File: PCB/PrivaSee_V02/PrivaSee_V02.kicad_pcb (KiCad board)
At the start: 2 copper layers, 76.2 x 101.6 mm, 18 parts, among them SW1 (Generic toggle state switch), U1 ESP32-C6-DevKitM-1, U2 LM358, U5 LM358

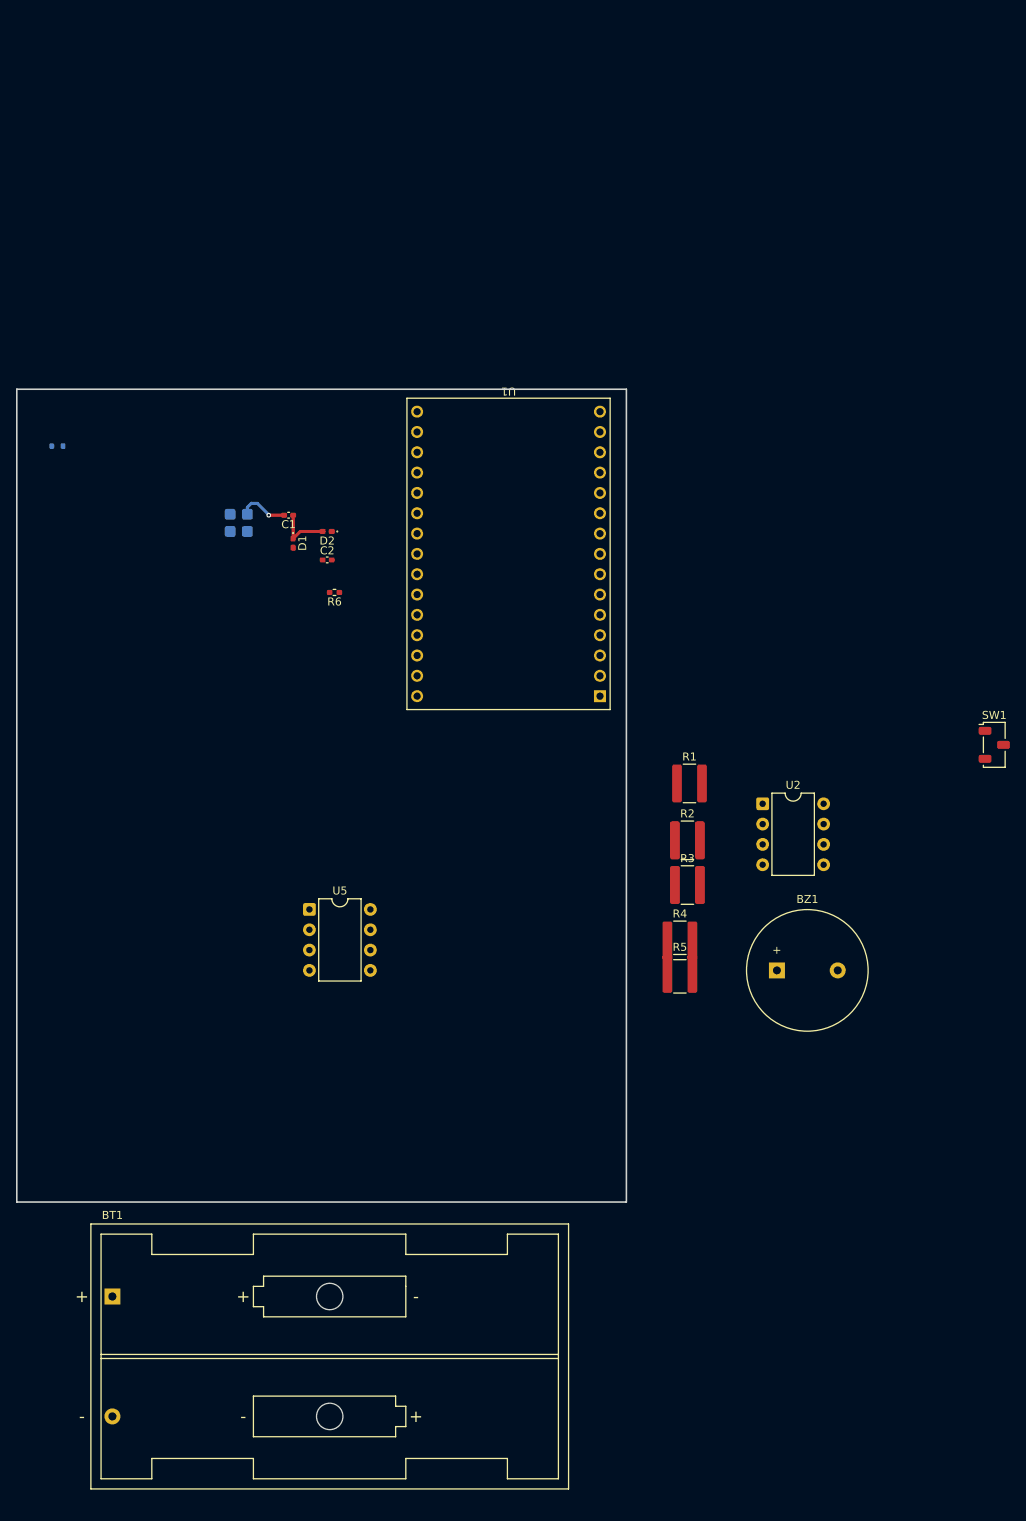
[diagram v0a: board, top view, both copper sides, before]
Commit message: PCB Layout Updates
Updated the footprint and the layout of the PCB
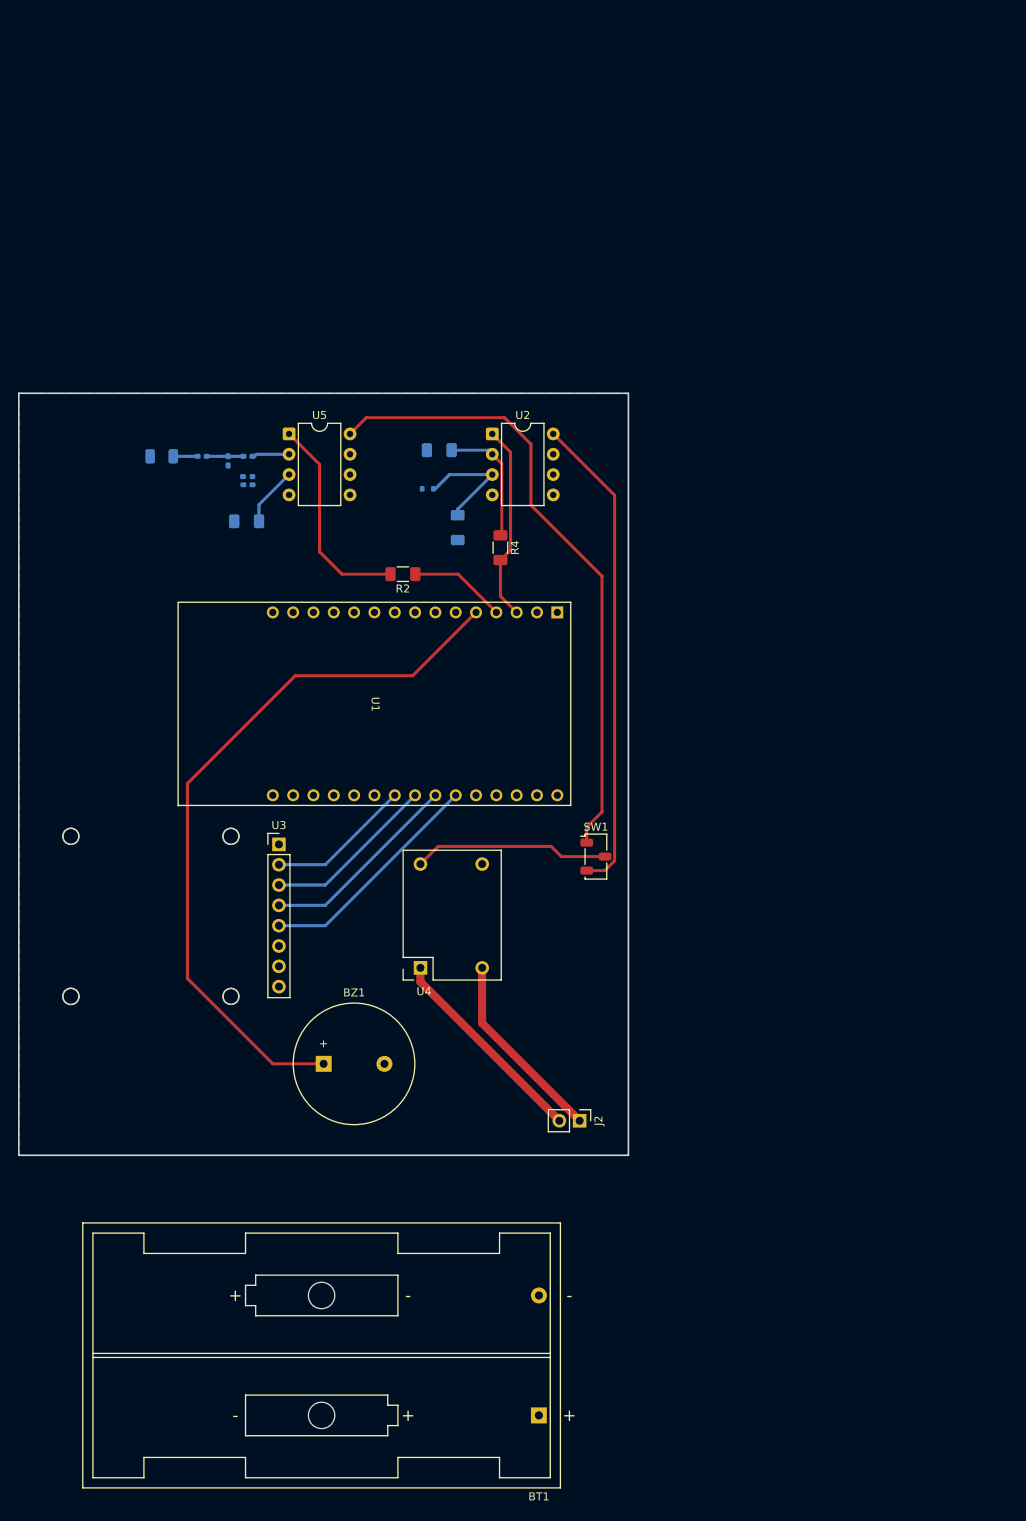
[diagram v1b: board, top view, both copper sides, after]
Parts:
- added J2: Batt_Solder_Point, Connector_PinHeader_2.54mm:PinHeader_1x02_P2.54mm_Vertical, F.Cu at (129.8, 112.5)
- added U3: 254, Connector_PinHeader_2.54mm:PinHeader_1x08_P2.54mm_Vertical, F.Cu at (92.2, 78.0)
- added U4: DFR0568, Connector_PinSocket_2.54mm:PinSocket_2x02_P2.54mm_Vertical, F.Cu at (109.1, 93.6)
- AE1: footprint RF_Antenna:Molex_47948-0001_2.4Ghz -> RF_Antenna:Johanson_2450AT18x100_2400-2500Mhz
- C1, C2, D1, D2, R6: moved to B.Cu
- R1, R3, R5: footprint Resistor_SMD:R_1218_3246Metric_Pad1.22x4.75mm_HandSolder -> Resistor_SMD:R_1206_3216Metric_Pad1.30x1.75mm_HandSolder; moved to B.Cu
- R2, R4: footprint Resistor_SMD:R_1218_3246Metric_Pad1.22x4.75mm_HandSolder -> Resistor_SMD:R_1206_3216Metric_Pad1.30x1.75mm_HandSolder
- moved R1 64.3 mm to (88.2, 37.6), turned to 180 degrees
- moved R3 62.6 mm to (112.2, 28.7)
- moved R5 62.3 mm to (114.6, 38.4), turned to 90 degrees
- moved U5 59.5 mm to (93.5, 26.7)
- moved BZ1 57.9 mm to (97.8, 105.4)
- moved U2 57.3 mm to (118.9, 26.7)
- moved BT1 55.3 mm to (124.7, 149.4), turned to 180 degrees
- moved R4 54.0 mm to (119.9, 40.9), turned to -90 degrees
- moved SW1 51.7 mm to (131.8, 79.5)
- moved R2 48.7 mm to (107.7, 44.2), turned to 180 degrees
- moved D3 46.6 mm to (110.8, 33.5)
- moved R6 18.1 mm to (88.3, 32.0)
- moved D2 13.7 mm to (88.3, 29.5)
- moved C2 13.7 mm to (88.3, 33.0)
- moved D1 13.1 mm to (85.9, 30.0)
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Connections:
- BZ1 pad 2: /GND -> GND
- C2 pad 1: /GND -> GND
- D1 pad 2: /GND -> GND
- D3 pad 2: /GND -> GND
- R1 pad 2: /GND -> GND
- R3 pad 1: /GND -> GND
- R5 pad 1: /GND -> GND
- R6 pad 2: /GND -> GND
- U1 pad 15: unconnected-(U1-GND-Pad15) -> GND
- U1 pad 16: unconnected-(U1-GND-Pad16) -> GND
- U1 pad 30: /GND -> GND
- U2 pad 4: /GND -> GND
- U5 pad 4: /GND -> GND
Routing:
- net Net-(BZ1-+): track 0.00 -> 90.7 mm
- net Net-(SW1-C): track 0.00 -> 79.1 mm
- net Net-(SW1-A): track 0.00 -> 60.5 mm
- net Net-(U1-GPIO21): track 0.00 -> 28.8 mm
- net Net-(R2-Pad2): track 0.00 -> 26.3 mm
- net Net-(BT1-+): track 0.00 -> 26.3 mm
- net Net-(U1-GPIO20): track 0.00 -> 25.3 mm
- net Net-(U1-GPIO2): track 0.00 -> 24.6 mm
- net Net-(SW1-B): track 0.00 -> 24.5 mm
- net Net-(BT1--): track 0.00 -> 24.2 mm
- net Net-(U1-GPIO19): track 0.00 -> 21.7 mm
- net Net-(U1-GPIO18): track 0.00 -> 18.1 mm
- net Net-(U2A--): track 0.00 -> 16.0 mm
- net Net-(D3-K): track 0.00 -> 15.0 mm
- net Net-(U1-GPIO3): track 0.00 -> 12.1 mm
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- added copper zone on B.Cu, net GND
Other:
- board size 76.2 x 101.6 mm -> 76.2 x 95.2 mm

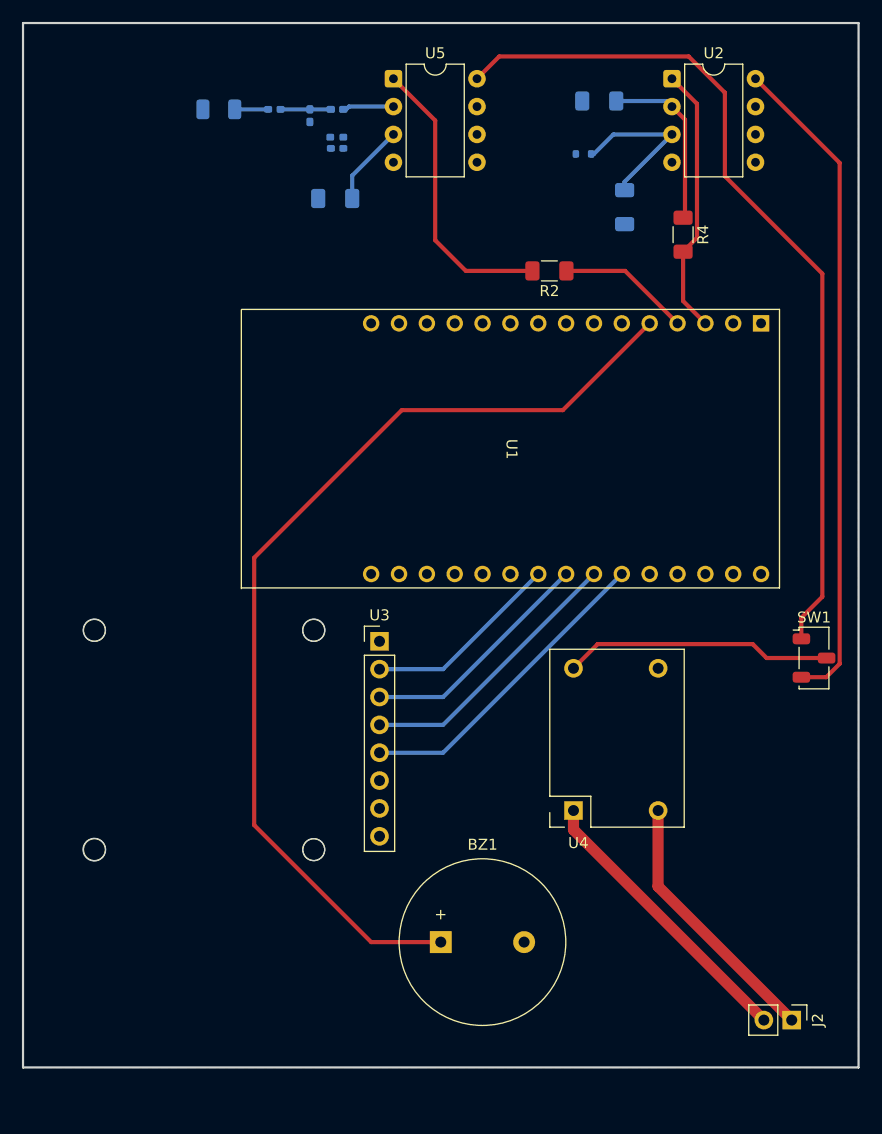
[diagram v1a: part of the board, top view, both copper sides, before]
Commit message: PCB Updates
I changed the PCB to match the footprints and make it a little bit smaller.
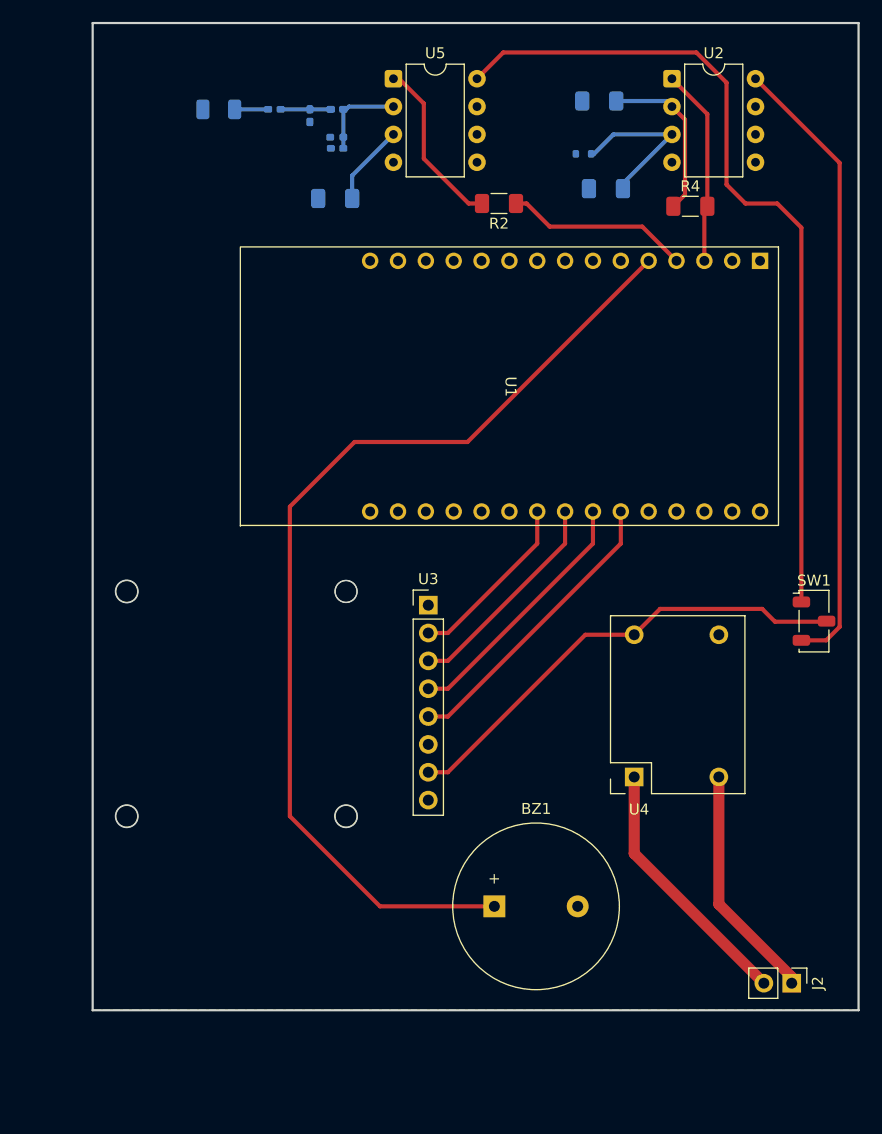
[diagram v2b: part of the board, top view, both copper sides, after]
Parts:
- moved R2 7.68 mm to (103.1, 38.0)
- moved U4 6.33 mm to (114.6, 90.5)
- moved BZ1 5.88 mm to (102.7, 102.1)
- moved U1 5.70 mm to (126.9, 43.3)
- moved U3 5.54 mm to (96.7, 74.7)
- moved J2 3.36 mm to (129.8, 109.2)
- moved SW1 3.36 mm to (131.8, 76.1)
- moved R4 2.67 mm to (120.5, 38.3), turned to 0 degrees
- moved R5 2.39 mm to (112.9, 36.7), turned to 0 degrees
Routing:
- net Net-(SW1-B): track 24.5 -> 43.0 mm
- net Net-(R2-Pad2): track 26.3 -> 15.7 mm
- net Net-(U1-GPIO2): track 24.6 -> 18.1 mm
- net Net-(U1-GPIO3): track 12.1 -> 16.8 mm
- net Net-(D2-K): track 5.04 -> 8.59 mm
- net Net-(SW1-A): track 60.5 -> 57.2 mm
- net Net-(BT1--): track 24.2 -> 21.6 mm
- net Net-(BT1-+): track 26.3 -> 23.7 mm
- net Net-(SW1-C): track 79.1 -> 76.8 mm
- net Net-(U1-GPIO20): track 25.3 -> 23.4 mm
- net Net-(U1-GPIO19): track 21.7 -> 19.8 mm
- net Net-(U1-GPIO21): track 28.8 -> 27.0 mm
- net Net-(BZ1-+): track 90.7 -> 92.3 mm
- net Net-(U1-GPIO18): track 18.1 -> 16.6 mm
- net Net-(U2A--): track 16.0 -> 15.3 mm
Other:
- board size 76.2 x 95.2 mm -> 69.8 x 90 mm

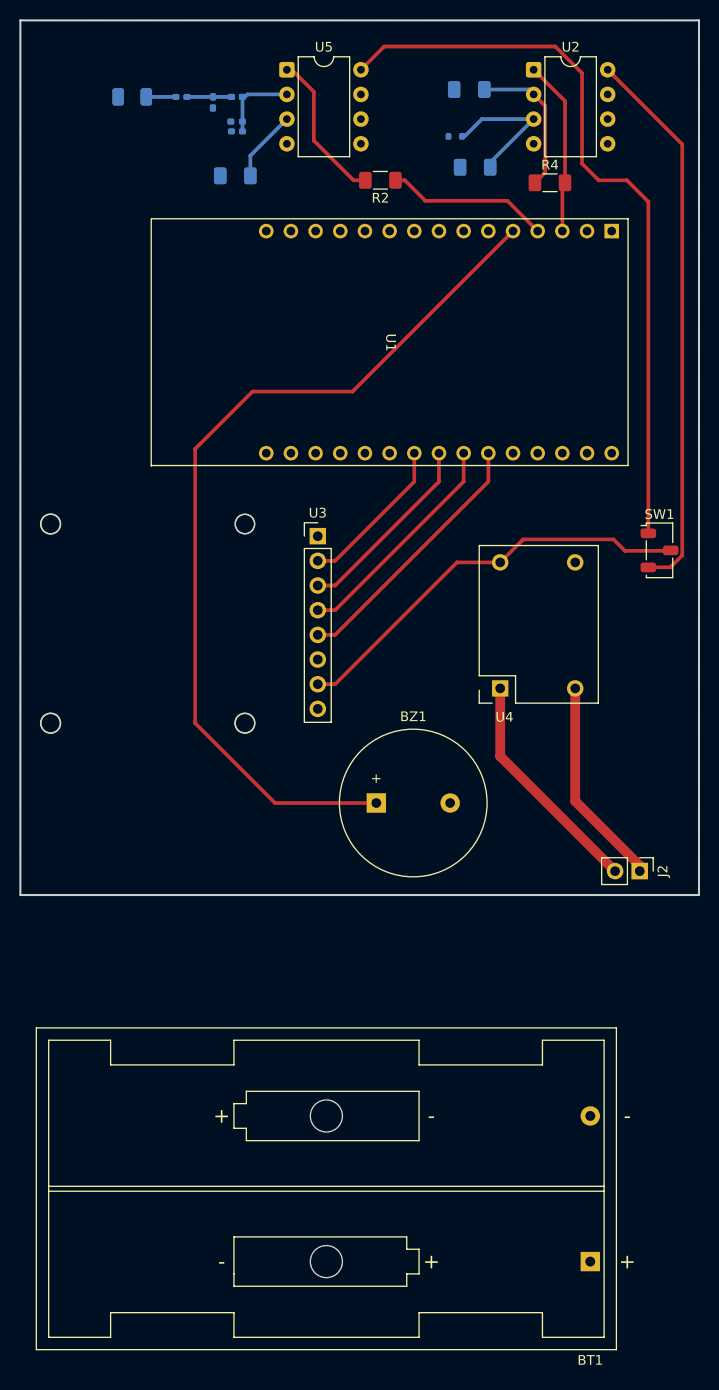
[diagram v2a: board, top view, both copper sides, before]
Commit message: PCB Updates
Changed ESP32 to C5, reoriented all components to hopefully reduce noise, and switched to 4 layers.
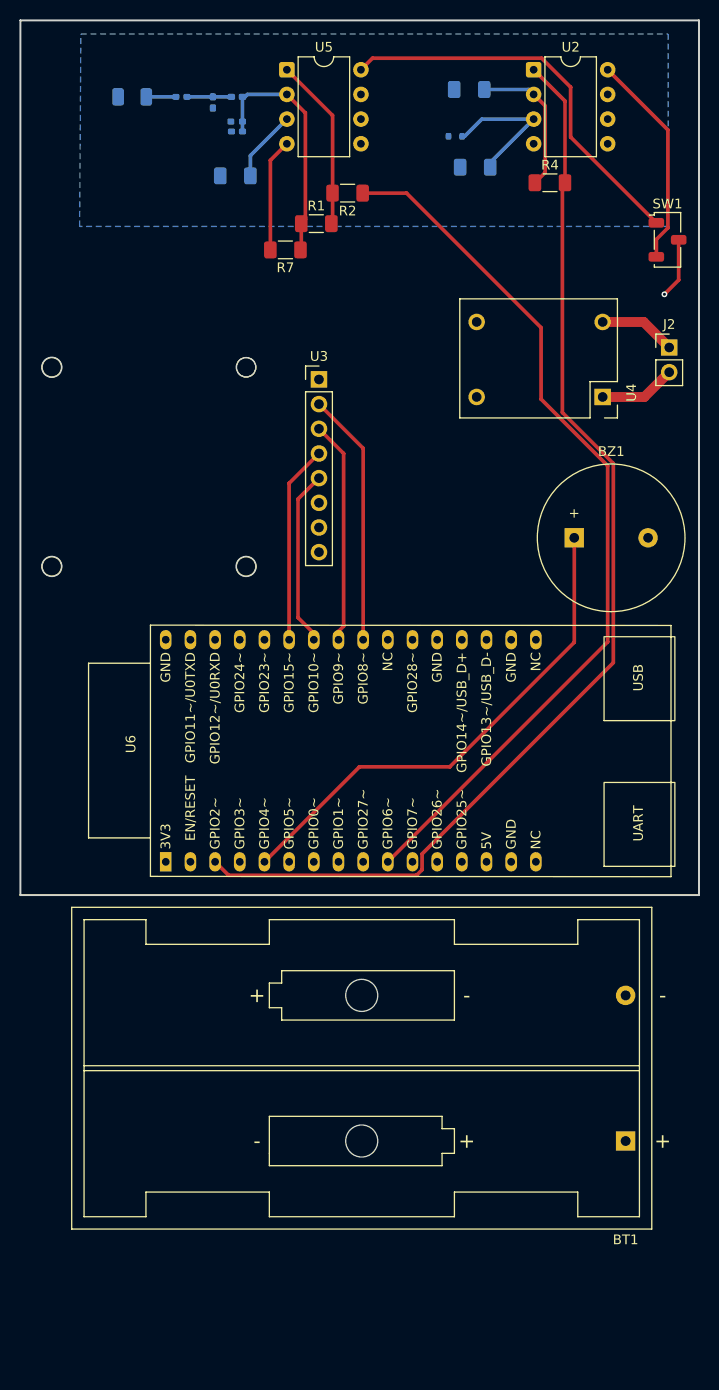
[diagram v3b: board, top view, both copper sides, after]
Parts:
- removed U1: ESP32-C6-DevKitM-1, RF_Module:ESP32-C3-DevKitM-1
- added R1: 100, Resistor_SMD:R_1206_3216Metric_Pad1.30x1.75mm_HandSolder, F.Cu at (96.5, 42.5)
- added R7: 10, Resistor_SMD:R_1206_3216Metric_Pad1.30x1.75mm_HandSolder, F.Cu at (93.3, 45.2)
- added U6: ESP32-C5-DevKitC-1, PCM_Espressif:ESP32-C5-DevKitC-1, F.Cu at (81.0, 108.2)
- moved J2 54.0 mm to (132.8, 55.3), turned to 0 degrees
- moved BZ1 34.1 mm to (123.0, 74.8)
- moved SW1 32.0 mm to (132.7, 44.2)
- moved U4 31.6 mm to (126.2, 61.2), turned to -90 degrees
- moved U3 16.1 mm to (96.8, 58.5)
- moved BT1 12.9 mm to (128.3, 136.9)
- moved R2 3.63 mm to (99.7, 39.4)
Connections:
- net Net-(SW1-B) renamed /3V3
- U5 pad 2: Net-(D2-K) -> Net-(U5A--)
- U5 pad 3: Net-(U5A-+) -> Net-(D2-K)
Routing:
- net Net-(U6-GPIO2/MTMS): track 18.1 -> 116.2 mm
- net Net-(U6-GPIO6): track 16.8 -> 91.3 mm
- net Net-(BZ1-+): track 92.3 -> 52.0 mm
- net Net-(SW1-C): track 76.8 -> 40.9 mm
- net Net-(SW1-A): track 57.2 -> 22.3 mm
- net /3V3: track 43.0 -> 9.04 mm, vias 0 -> 1
- net Net-(U5A--): track 0.00 -> 17.0 mm
- net Net-(BT1-+): track 23.7 -> 7.91 mm
- net Net-(BT1--): track 21.6 -> 7.94 mm
- net GND: track 0.00 -> 11.6 mm
- net Net-(U3-CS): track 16.6 -> 26.1 mm
- net Net-(U3-CLK): track 27.0 -> 18.2 mm
- net Net-(U3-DI): track 19.8 -> 23.0 mm
- net Net-(U3-DO): track 23.4 -> 20.4 mm
- net Net-(R1-Pad2): track 15.7 -> 17.8 mm
- added copper zone on In1.Cu, net /3V3
- added copper zone on In2.Cu, net GND
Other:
- copper layers 2 -> 4
